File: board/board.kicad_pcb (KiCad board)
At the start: 4 copper layers, 21 x 77 mm, 74 parts, among them J1 UART, J2 008_USB, J3 DebugEdge_02x05, J4 019_100BASE-T_with_CT, J5 ADC_2x3, J6 SWD_6_Pol_Needle, J7 SPI_2x3, J8 I2C_2x2, J9 UART_2x2, SW1 PTS636 SK25J SMTR LFS, U1 W25Q16JVUXIQ, U2 RP2040, U3 W5500, U4 11AA02E48, Y1 12MhZ, Y2 25MHz

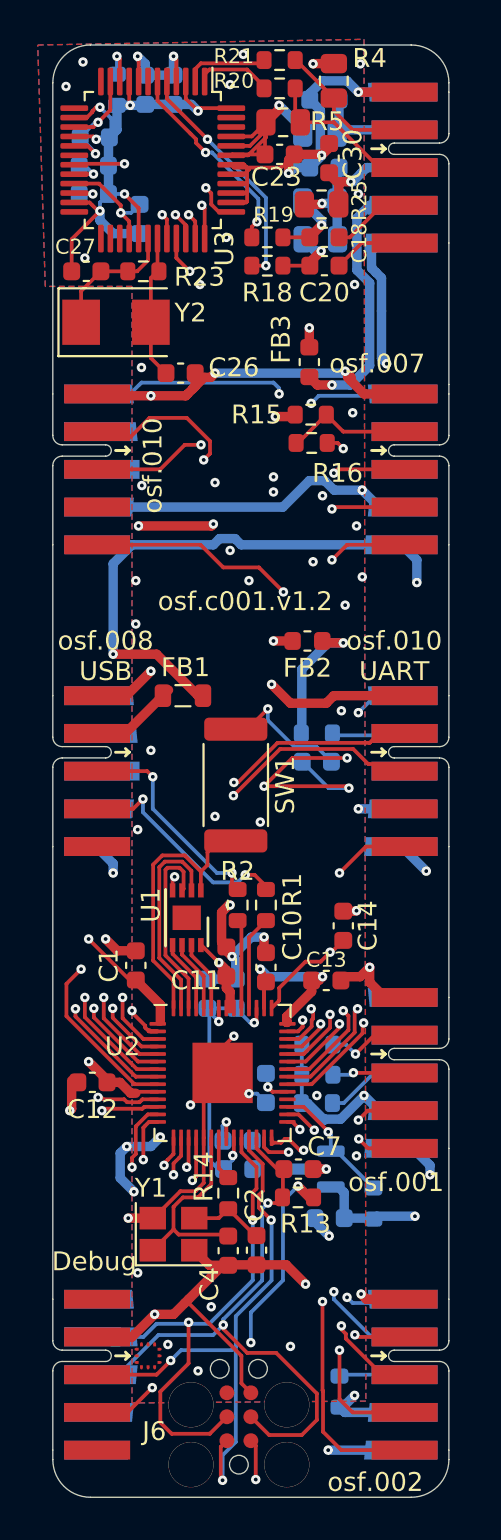
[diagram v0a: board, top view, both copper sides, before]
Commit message: fixed I2C pinning defect
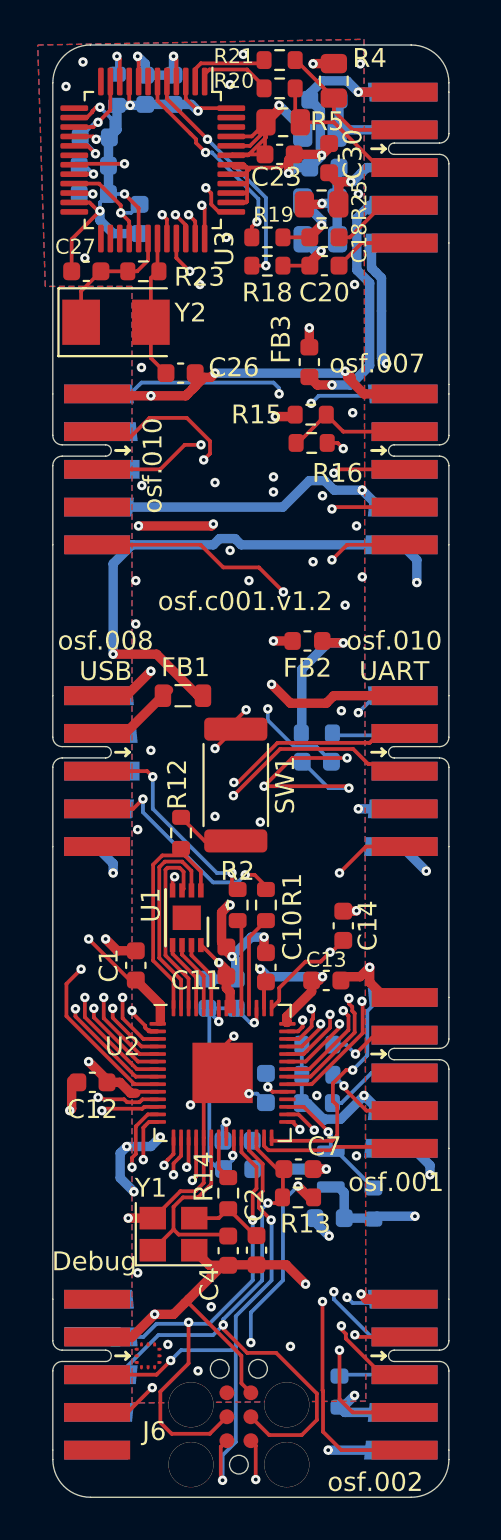
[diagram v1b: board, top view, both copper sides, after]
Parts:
- added R12: 1k, Resistor_SMD:R_0603_1608Metric, F.Cu at (146.8, 67.8)
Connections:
- J8 pad 3: /I2C1_SCL -> unconnected-(J8-N/C-Pad3)
- J8 pad 4: /GPIO16 -> /I2C1_SCL
- J8 pad 5: /GPIO17 -> /GPIO16
- J8 pad 6: (no net) -> /GPIO17
- J8 pad 7: (no net) -> unconnected-(J8-status-Pad7)
- SW1 pad 1: /uC3.3V -> GND
- SW1 pad 2: /rp2040/QPI_SS -> Net-(R12-Pad1)
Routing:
- net /GPIO17: track 8.04 -> 13.6 mm, vias 2 -> 1
- net Net-(R12-Pad1): track 0.00 -> 3.42 mm
- net /rp2040/QPI_SS: track 15.1 -> 12.1 mm
- net GND: track 315.8 -> 318.6 mm, vias 75 -> 77
- net /uC3.3V: track 169.6 -> 167.5 mm
- net /GPIO16: track 8.97 -> 8.09 mm, vias 2 -> 0

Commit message: moved all components to top layer
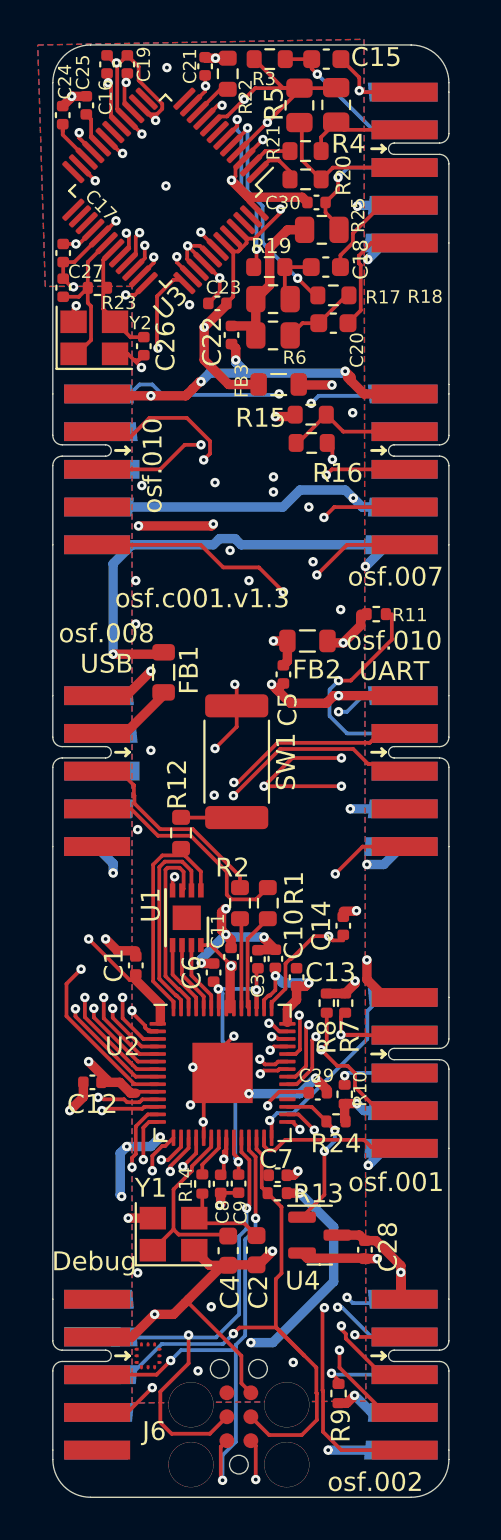
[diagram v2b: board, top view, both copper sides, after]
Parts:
- C1, C10, C11, C12, C13, C14, C23, C26, C27, C30, C7: footprint Capacitor_SMD:C_0603_1608Metric -> Capacitor_SMD:C_0402_1005Metric
- C15, R17, R22, R6, U4: moved to F.Cu
- C16, C17, C19, C21, C22, C24, C28, C29, C3, C5, C6, C8, C9: footprint Capacitor_SMD:C_0603_1608Metric -> Capacitor_SMD:C_0402_1005Metric; moved to F.Cu
- C25: value 4.7u -> 4.7uF; footprint Capacitor_SMD:C_0603_1608Metric -> Capacitor_SMD:C_0402_1005Metric; moved to F.Cu
- FB2, FB3: footprint Inductor_SMD:L_0603_1608Metric -> Inductor_SMD:L_0805_2012Metric
- R10, R11, R24, R7, R8, R9: footprint Resistor_SMD:R_0603_1608Metric -> Resistor_SMD:R_0402_1005Metric; moved to F.Cu
- R13, R14, R23: footprint Resistor_SMD:R_0603_1608Metric -> Resistor_SMD:R_0402_1005Metric
- R3: footprint Resistor_SMD:R_0805_2012Metric -> Resistor_SMD:R_0603_1608Metric; moved to F.Cu
- Y2: value 25MHz -> 25MhZ; footprint Crystal:Crystal_SMD_5032-2Pin_5.0x3.2mm -> Crystal:Crystal_SMD_Abracon_ABM8G-4Pin_3.2x2.5mm
- moved C22 10.1 mm to (149.5, 41.4), turned to -90 degrees
- moved C23 8.56 mm to (148.7, 39.7), turned to 180 degrees
- moved C16 8.37 mm to (142.9, 27.0), turned to 90 degrees
- moved R11 7.07 mm to (157.2, 56.2)
- moved C17 6.35 mm to (140.6, 37.0), turned to -90 degrees
- moved R22 5.94 mm to (149.3, 27.5), turned to 90 degrees
- moved R17 5.74 mm to (151.7, 39.5), turned to 0 degrees
- moved R6 5.69 mm to (151.7, 41.4), turned to 0 degrees
- moved R20 5.02 mm to (153.4, 33.1)
- moved R21 5.02 mm to (153.4, 31.6)
- moved C5 4.96 mm to (152.2, 59.4), turned to -90 degrees
- moved R24 4.78 mm to (155.0, 83.1), turned to 180 degrees
- moved R3 4.76 mm to (151.5, 26.8)
- moved C24 4.49 mm to (140.5, 29.7), turned to -90 degrees
- moved R18 3.84 mm to (154.9, 39.3)
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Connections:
- Y2 pad 2: /controller/XO -> GND
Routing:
- net GND: track 318.6 -> 352.9 mm
- net +3.3V: track 124.9 -> 108.0 mm, vias 7 -> 9
- net /rp2040/GPIO7: track 58.5 -> 48.8 mm
- net /rp2040/GPIO6: track 55.9 -> 48.3 mm
- net Net-(J9-~{RESET}): track 3.91 -> 11.5 mm, vias 0 -> 1
- net /I2C1_SCL: track 9.61 -> 16.7 mm
- net +5V: track 127.4 -> 120.4 mm
- net /GPIO24: track 44.5 -> 39.2 mm
- net /controller/VDD: track 78.9 -> 74.2 mm, vias 8 -> 9
- net Net-(U2-VREG_VOUT): track 16.2 -> 19.4 mm
- net /rp2040/SPI0_SCK: track 47.1 -> 50.1 mm
- net /GPIO25: track 51.0 -> 48.2 mm
- net /controller/CT1: track 5.50 -> 8.17 mm, vias 0 -> 1
- net /controller/RXN: track 3.97 -> 6.60 mm
- net Net-(C22-Pad1): track 5.65 -> 7.96 mm, vias 1 -> 0
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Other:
- board text added: "osf.c001.v1.3"
- board text removed: "osf.c001.v1.2"
